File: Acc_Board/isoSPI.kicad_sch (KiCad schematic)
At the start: 11 parts, among them J4 IsoSPI, U2 LTC6820

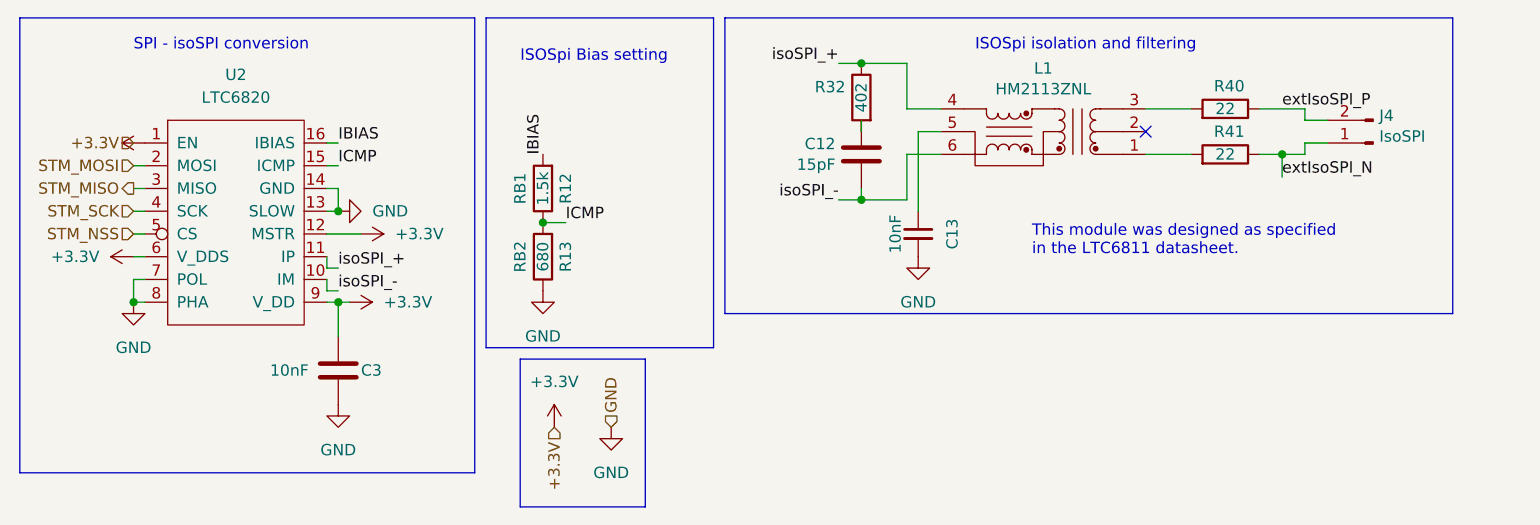
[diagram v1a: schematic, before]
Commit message: Removed ACC parts from BSPD board and organized ACC board schematic
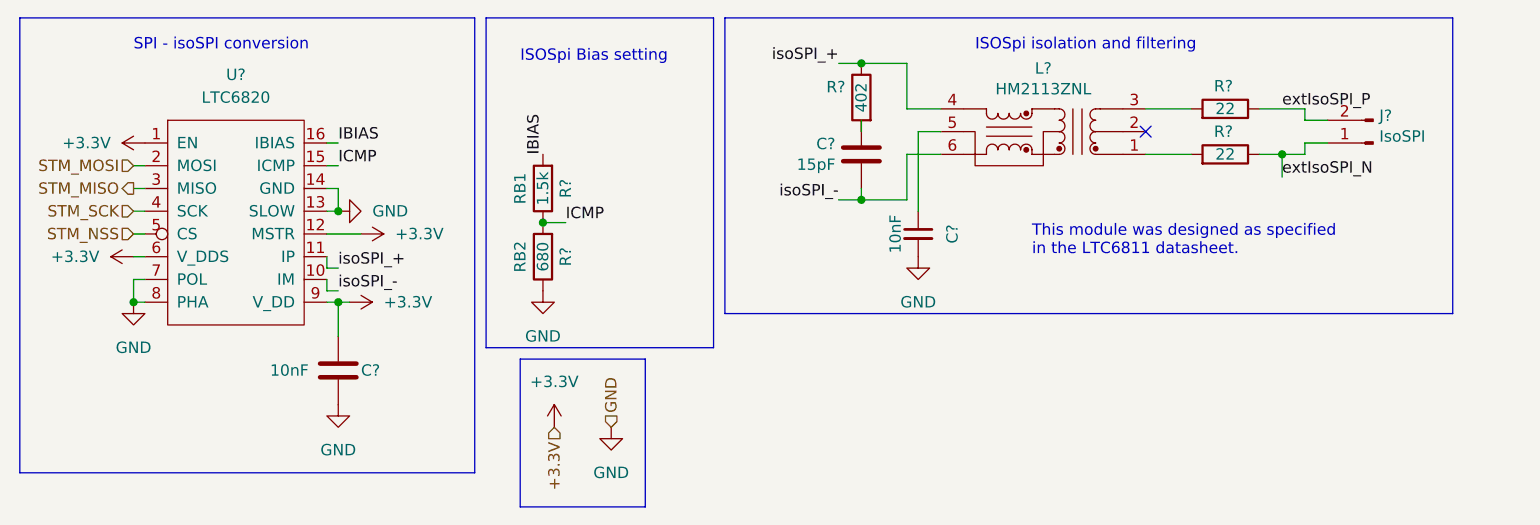
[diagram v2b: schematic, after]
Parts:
- renumbered C12 to C?, C13 to C?, C3 to C?, J4 to J?, L1 to L?, R32 to R?, R41 to R?, R12 to R?, R13 to R?, R40 to R?, U2 to U?

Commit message: Added most footprints to ACC board
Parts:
- L?: footprint FSFootprints:HM2113ZNL -> 1FS_2_Global_Footprint_Library:HM2113ZNL
- U?: footprint PCM_Package_SO_AKL:MSOP-16_3x4mm_P0.5mm -> 1FS_2_Global_Footprint_Library:MSOP-16_[LTC6820]_10_thou_compat
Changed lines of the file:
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@@
       (effects (font (size 1.27 1.27)))
     )
-    (property "Footprint" "PCM_Package_SO_AKL:MSOP-16_3x4mm_P0.5mm" (at 46.99 29.21 0)
+    (property "Footprint" "1FS_2_Global_Footprint_Library:MSOP-16_[LTC6820]_10_thou_compat" (at 46.99 29.21 0)
       (effects (font (size 1.27 1.27)) hide)
     )
@@
       (effects (font (size 1.27 1.27)))
     )
-    (property "Footprint" "FSFootprints:HM2113ZNL" (at 133.35 34.29 0)
+    (property "Footprint" "1FS_2_Global_Footprint_Library:HM2113ZNL" (at 133.35 34.29 0)
       (effects (font (size 1.27 1.27)) hide)
     )

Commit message: Minor acc board changes
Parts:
- C? (x3): footprint Capacitor_SMD:C_0805_2012Metric_Pad1.18x1.45mm_HandSolder -> (none)
- R? (x5): footprint Resistor_SMD:R_0805_2012Metric_Pad1.20x1.40mm_HandSolder -> (none)
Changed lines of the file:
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@@
       (effects (font (size 1.27 1.27)) (justify right))
     )
-    (property "Footprint" "Capacitor_SMD:C_0805_2012Metric_Pad1.18x1.45mm_HandSolder" (at 117.8052 33.02 0)
+    (property "Footprint" "" (at 117.8052 33.02 0)
       (effects (font (size 1.27 1.27)) hide)
     )
@@
       (effects (font (size 1.27 1.27)))
     )
-    (property "Footprint" "Resistor_SMD:R_0805_2012Metric_Pad1.20x1.40mm_HandSolder" (at 118.618 30.48 90)
+    (property "Footprint" "" (at 118.618 30.48 90)
       (effects (font (size 1.27 1.27)) hide)
     )
@@
       (effects (font (size 1.27 1.27)))
     )
-    (property "Footprint" "Capacitor_SMD:C_0805_2012Metric_Pad1.18x1.45mm_HandSolder" (at 124.1552 49.53 0)
+    (property "Footprint" "" (at 124.1552 49.53 0)
       (effects (font (size 1.27 1.27)) hide)
     )
@@
       (effects (font (size 1.27 1.27)))
     )
-    (property "Footprint" "Resistor_SMD:R_0805_2012Metric_Pad1.20x1.40mm_HandSolder" (at 157.48 38.608 90)
+    (property "Footprint" "" (at 157.48 38.608 90)
       (effects (font (size 1.27 1.27)) hide)
     )
@@
       (effects (font (size 1.27 1.27)) (justify left))
     )
-    (property "Footprint" "Capacitor_SMD:C_0805_2012Metric_Pad1.18x1.45mm_HandSolder" (at 59.3852 64.77 0)
+    (property "Footprint" "" (at 59.3852 64.77 0)
       (effects (font (size 1.27 1.27)) hide)
     )
@@
       (effects (font (size 1.27 1.27)))
     )
-    (property "Footprint" "Resistor_SMD:R_0805_2012Metric_Pad1.20x1.40mm_HandSolder" (at 81.28 40.64 0)
+    (property "Footprint" "" (at 81.28 40.64 0)
       (effects (font (size 1.27 1.27)) hide)
     )
@@
       (effects (font (size 1.27 1.27)))
     )
-    (property "Footprint" "Resistor_SMD:R_0805_2012Metric_Pad1.20x1.40mm_HandSolder" (at 83.058 48.26 90)
+    (property "Footprint" "" (at 83.058 48.26 90)
       (effects (font (size 1.27 1.27)) hide)
     )
@@
       (effects (font (size 1.27 1.27)))
     )
-    (property "Footprint" "Resistor_SMD:R_0805_2012Metric_Pad1.20x1.40mm_HandSolder" (at 157.48 33.528 90)
-      (effects (font (size 1.27 1.27)) hide)
-    )
+    (property "Footprint" "" (at 157.48 33.528 90)
+      (effects (font (size 1.27 1.27)) hide)
+    )

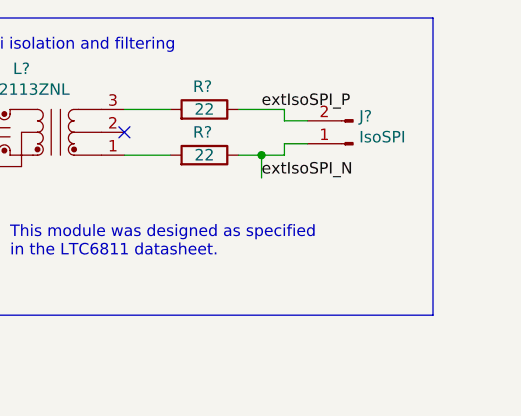
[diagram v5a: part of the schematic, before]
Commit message: changed BMU connector to 180 degree version and named connectors
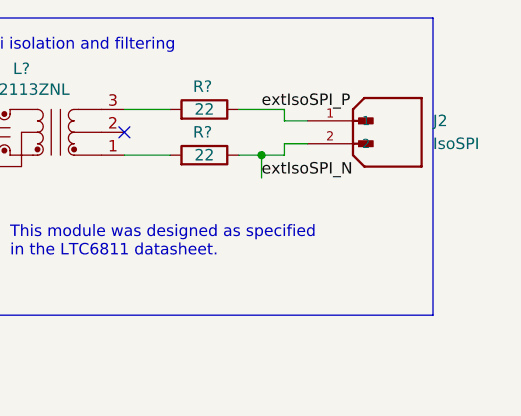
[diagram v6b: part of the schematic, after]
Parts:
- removed J?: IsoSPI, Connector_Molex:Molex_Nano-Fit_105313-xx02_1x02_P2.50mm_Horizontal, symbol Connector:Conn_01x02_Pin
- added J2: IsoSPI, 1053091202:MOLEX_1053091202, symbol 1FS_2_Global_Symbol_Library:1053091202
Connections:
- net extIsoSPI_N: now also J2.2
- net extIsoSPI_P: now also J2.1
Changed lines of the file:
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@@
     (effects (font (size 1.27 1.27)) (justify left))
-  )
-  (symbol (lib_id "Connector:Conn_01x02_Pin") (at 173.99 35.56 180) (unit 1)
-    (in_bom yes) (on_board yes) (dnp no)
-    (property "Reference" "J?" (at 174.6758 32.512 0)
-      (effects (font (size 1.27 1.27)) (justify right))
-    )
-    (property "Value" "IsoSPI" (at 174.6758 34.8234 0)
-      (effects (font (size 1.27 1.27)) (justify right))
-    )
-    (property "Footprint" "Connector_Molex:Molex_Nano-Fit_105313-xx02_1x02_P2.50mm_Horizontal" (at 173.99 35.56 0)
-      (effects (font (size 1.27 1.27)) hide)
-    )
-    (property "Datasheet" "~" (at 173.99 35.56 0)
-      (effects (font (size 1.27 1.27)) hide)
-    )
-    (pin "1")
-    (pin "2")
-    (instances
-      (project "BMS"
-        (path "/72dffc1c-220a-4c2e-8170-16d349f136df"
-          (reference "J?") (unit 1)
-        )
-      )
-      (project "BMS_Controller"
-        (path "/cb6c61fd-673a-449c-8134-4a1c25621518"
-          (reference "J?") (unit 1)
-        )
-        (path "/cb6c61fd-673a-449c-8134-4a1c25621518/faa386f8-35fb-44d9-8ccf-12944498b7dc"
-          (reference "J?") (unit 1)
-        )
-      )
-      (project "Acc_Board"
-        (path "/e19d26dd-723b-45e6-9d59-b1730158e759/418586a7-bc6a-480e-8435-4a2eb96d1e0c"
-          (reference "J7") (unit 1)
-        )
-      )
-    )
   )
   (symbol (lib_id "Device:C") (at 116.84 36.83 0) (mirror x) (unit 1)
@@
         )
       )
+    )
+  )
+  (symbol (lib_id "1FS_2_Global_Symbol_Library:1053091202") (at 173.99 33.02 0) (unit 1)
+    (in_bom yes) (on_board yes) (dnp no) (fields_autoplaced)
+    (property "Reference" "J2" (at 182.88 33.02 0)
+      (effects (font (size 1.27 1.27)) (justify left))
+    )
+    (property "Value" "IsoSPI" (at 182.88 35.56 0)
+      (effects (font (size 1.27 1.27)) (justify left))
+    )
+    (property "Footprint" "1053091202:MOLEX_1053091202" (at 173.99 33.02 0)
+      (effects (font (size 1.27 1.27)) (justify bottom) hide)
+    )
+    (property "Datasheet" "" (at 173.99 33.02 0)
+      (effects (font (size 1.27 1.27)) hide)
+    )
+    (property "PARTREV" "H" (at 173.99 33.02 0)
+      (effects (font (size 1.27 1.27)) (justify bottom) hide)
+    )
+    (property "STANDARD" "Manufacturer Recommendations" (at 173.99 33.02 0)
+      (effects (font (size 1.27 1.27)) (justify bottom) hide)
+    )
+    (property "MAXIMUM_PACKAGE_HEIGHT" "10.51 mm" (at 173.99 33.02 0)
+      (effects (font (size 1.27 1.27)) (justify bottom) hide)
+    )
+    (property "MANUFACTURER" "Molex" (at 173.99 33.02 0)
+      (effects (font (size 1.27 1.27)) (justify bottom) hide)
+    )
+    (pin "2")
+    (pin "1")
+    (instances
+      (project "Acc_Board"
+        (path "/e19d26dd-723b-45e6-9d59-b1730158e759/418586a7-bc6a-480e-8435-4a2eb96d1e0c"
+          (reference "J2") (unit 1)
+        )
+      )

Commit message: Added footprints for resistors and capacitors
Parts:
- C? (x3): footprint (none) -> Capacitor_SMD:C_0805_2012Metric_Pad1.18x1.45mm_HandSolder
- R? (x5): footprint (none) -> Resistor_SMD:R_0805_2012Metric_Pad1.20x1.40mm_HandSolder
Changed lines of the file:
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@@
       (effects (font (size 1.27 1.27)) (justify right))
     )
-    (property "Footprint" "" (at 117.8052 33.02 0)
+    (property "Footprint" "Capacitor_SMD:C_0805_2012Metric_Pad1.18x1.45mm_HandSolder" (at 117.8052 33.02 0)
       (effects (font (size 1.27 1.27)) hide)
     )
@@
       (effects (font (size 1.27 1.27)))
     )
-    (property "Footprint" "" (at 118.618 30.48 90)
+    (property "Footprint" "Resistor_SMD:R_0805_2012Metric_Pad1.20x1.40mm_HandSolder" (at 118.618 30.48 90)
       (effects (font (size 1.27 1.27)) hide)
     )
@@
       (effects (font (size 1.27 1.27)))
     )
-    (property "Footprint" "" (at 124.1552 49.53 0)
+    (property "Footprint" "Capacitor_SMD:C_0805_2012Metric_Pad1.18x1.45mm_HandSolder" (at 124.1552 49.53 0)
       (effects (font (size 1.27 1.27)) hide)
     )
@@
       (effects (font (size 1.27 1.27)))
     )
-    (property "Footprint" "" (at 157.48 38.608 90)
+    (property "Footprint" "Resistor_SMD:R_0805_2012Metric_Pad1.20x1.40mm_HandSolder" (at 157.48 38.608 90)
       (effects (font (size 1.27 1.27)) hide)
     )
@@
       (effects (font (size 1.27 1.27)) (justify left))
     )
-    (property "Footprint" "" (at 59.3852 64.77 0)
+    (property "Footprint" "Capacitor_SMD:C_0805_2012Metric_Pad1.18x1.45mm_HandSolder" (at 59.3852 64.77 0)
       (effects (font (size 1.27 1.27)) hide)
     )
@@
       (effects (font (size 1.27 1.27)))
     )
-    (property "Footprint" "" (at 81.28 40.64 0)
+    (property "Footprint" "Resistor_SMD:R_0805_2012Metric_Pad1.20x1.40mm_HandSolder" (at 81.28 40.64 0)
       (effects (font (size 1.27 1.27)) hide)
     )
@@
       (effects (font (size 1.27 1.27)))
     )
-    (property "Footprint" "" (at 83.058 48.26 90)
+    (property "Footprint" "Resistor_SMD:R_0805_2012Metric_Pad1.20x1.40mm_HandSolder" (at 83.058 48.26 90)
       (effects (font (size 1.27 1.27)) hide)
     )
@@
       (effects (font (size 1.27 1.27)))
     )
-    (property "Footprint" "" (at 157.48 33.528 90)
-      (effects (font (size 1.27 1.27)) hide)
-    )
+    (property "Footprint" "Resistor_SMD:R_0805_2012Metric_Pad1.20x1.40mm_HandSolder" (at 157.48 33.528 90)
+      (effects (font (size 1.27 1.27)) hide)
+    )

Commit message: Changed power block and HVIL power
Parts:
- J2: footprint 1053091202:MOLEX_1053091202 -> 1FS_2_Global_Footprint_Library:MOLEX_1053091202
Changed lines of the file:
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@@
       (effects (font (size 1.27 1.27)) (justify left))
     )
-    (property "Footprint" "1053091202:MOLEX_1053091202" (at 173.99 33.02 0)
+    (property "Footprint" "1FS_2_Global_Footprint_Library:MOLEX_1053091202" (at 173.99 33.02 0)
       (effects (font (size 1.27 1.27)) (justify bottom) hide)
     )
